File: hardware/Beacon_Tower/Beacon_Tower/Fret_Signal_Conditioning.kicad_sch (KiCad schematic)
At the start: 4 parts

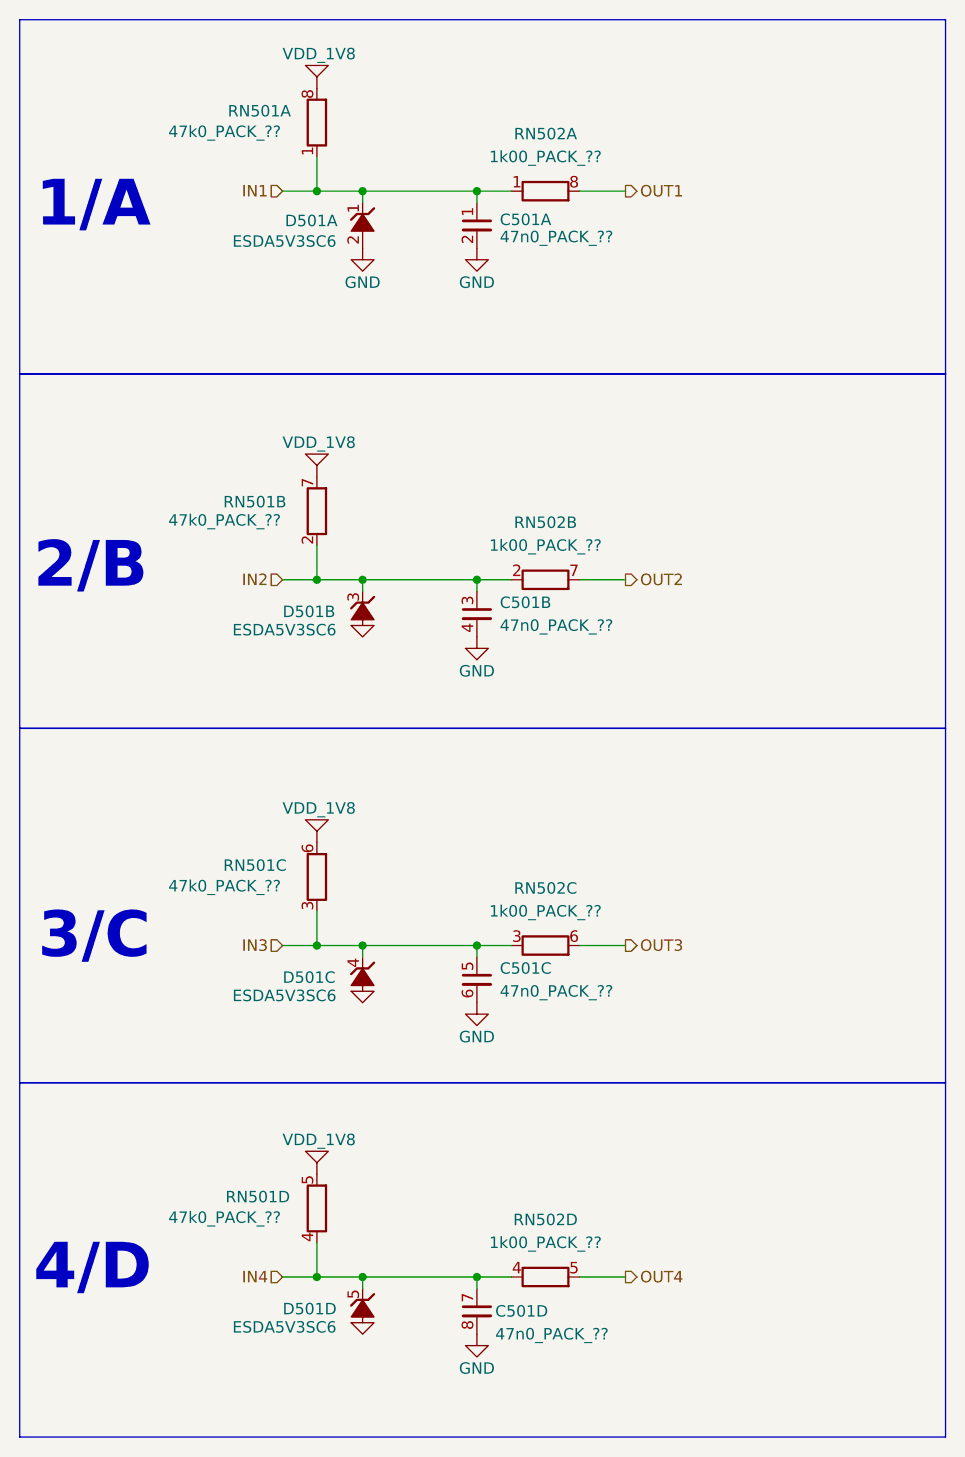
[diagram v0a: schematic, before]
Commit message: Started assigning footprints. Tweaking schematic.
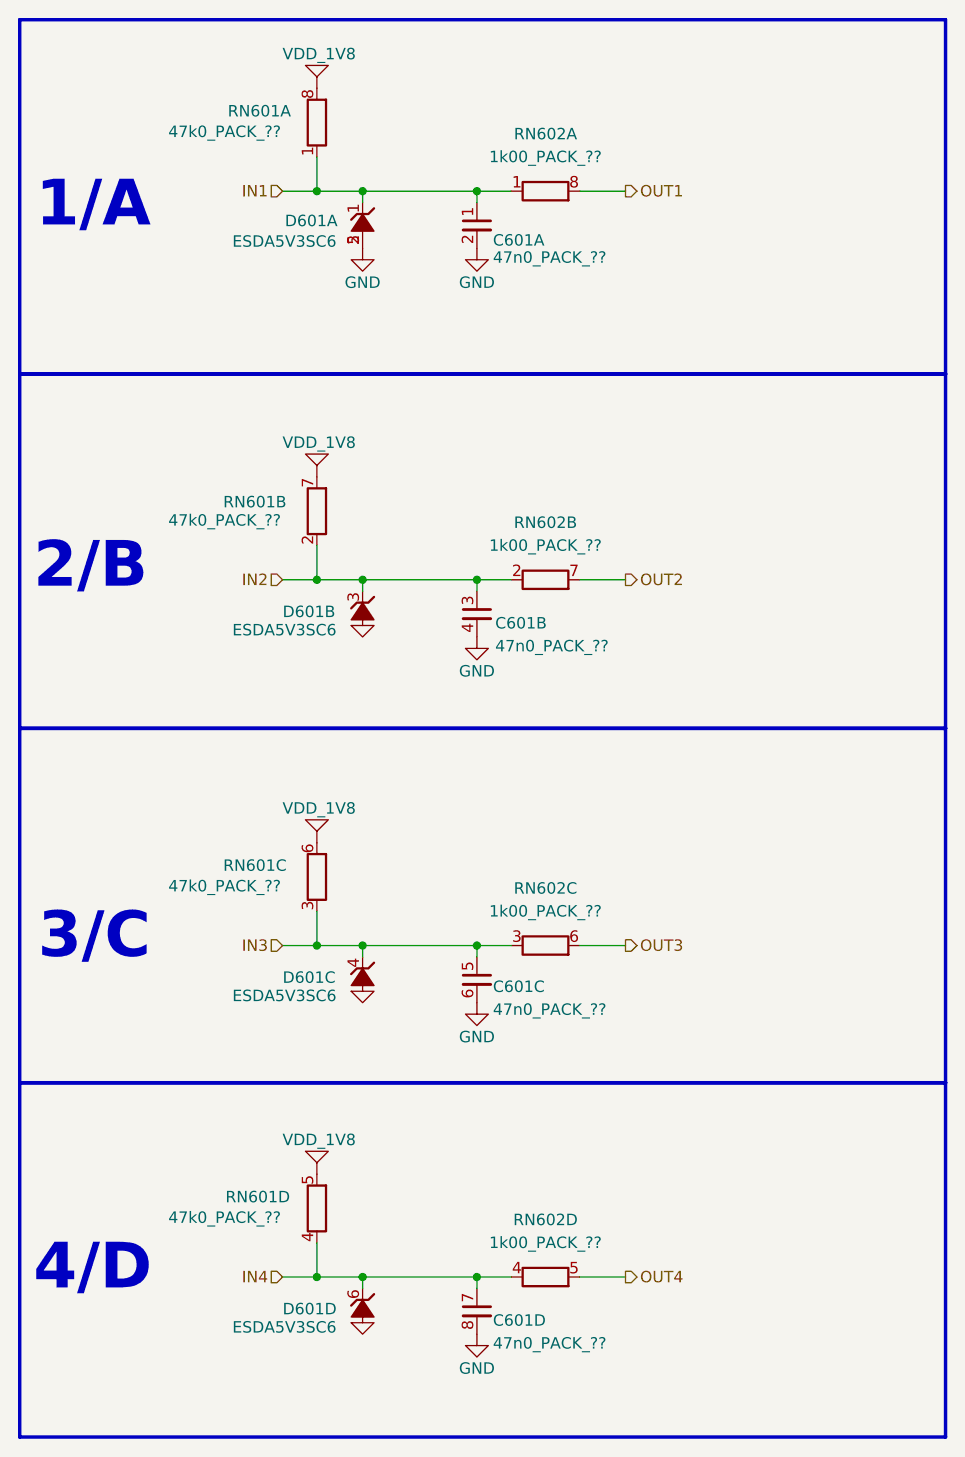
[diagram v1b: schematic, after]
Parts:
- D601: renamed from D501; footprint (none) -> Package_TO_SOT_SMD:SOT-23-6
- renumbered C501 to C601, D501 to D601, RN501 to RN601, RN502 to RN602
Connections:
- net GND: now also D601.5
- net IN4: now also D601.6; no longer D601.5
